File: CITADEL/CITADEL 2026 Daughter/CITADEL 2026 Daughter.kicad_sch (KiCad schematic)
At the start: 4 parts, among them J1 Servo_Daughter

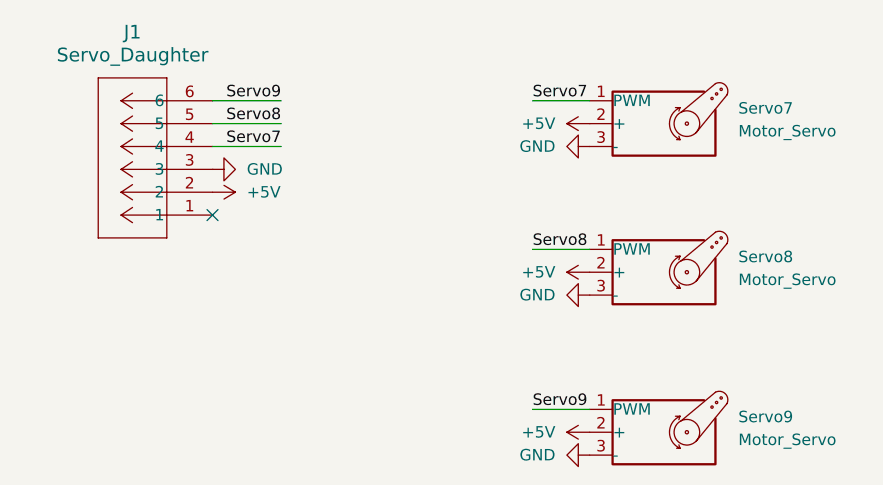
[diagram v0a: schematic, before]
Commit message: Updated servo connectors
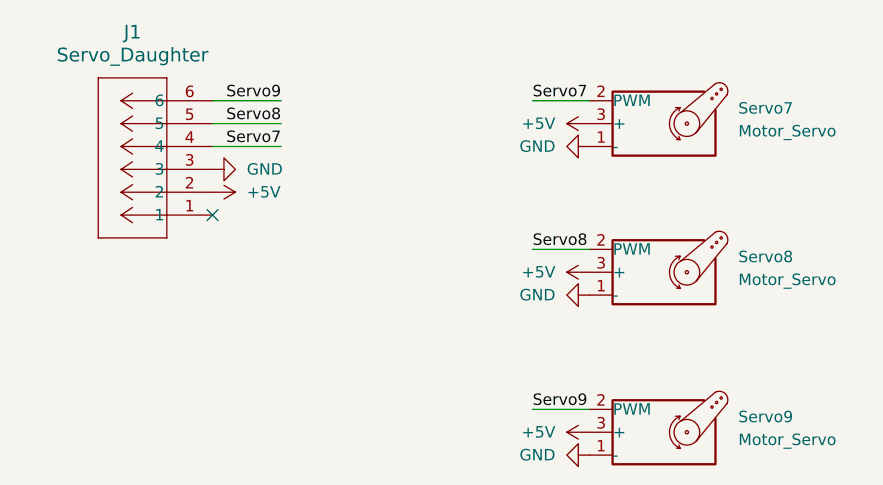
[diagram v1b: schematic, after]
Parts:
- Servo7, Servo8, Servo9: footprint Connector_PinHeader_2.54mm:PinHeader_1x03_P2.54mm_Vertical -> Connector_Molex:Molex_Mini-Fit_Jr_5566-04A_2x02_P4.20mm_Vertical
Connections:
- net +5V: now also Servo7.3 (+), Servo8.3 (+), Servo9.3 (+); no longer Servo7.2 (+), Servo8.2 (+), Servo9.2 (+)
- net GND: now also Servo7.1 (-), Servo8.1 (-), Servo9.1 (-); no longer Servo7.3 (-), Servo8.3 (-), Servo9.3 (-)
- net Servo7: now also Servo7.2 (PWM); no longer Servo7.1 (PWM)
- net Servo8: now also Servo8.2 (PWM); no longer Servo8.1 (PWM)
- net Servo9: now also Servo9.2 (PWM); no longer Servo9.1 (PWM)
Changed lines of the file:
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@@
 	)
 	(symbol
+		(lib_name "Motor_Servo_2")
 		(lib_id "Motor:Motor_Servo")
 		(at 90.17 49.53 0)
@@
 			)
 		)
-		(property "Footprint" "Connector_PinHeader_2.54mm:PinHeader_1x03_P2.54mm_Vertical"
+		(property "Footprint" "Connector_Molex:Molex_Mini-Fit_Jr_5566-04A_2x02_P4.20mm_Vertical"
 			(at 90.17 54.356 0)
 			(effects
@@
 	)
 	(symbol
+		(lib_name "Motor_Servo_1")
 		(lib_id "Motor:Motor_Servo")
 		(at 90.17 33.02 0)
@@
 			)
 		)
-		(property "Footprint" "Connector_PinHeader_2.54mm:PinHeader_1x03_P2.54mm_Vertical"
+		(property "Footprint" "Connector_Molex:Molex_Mini-Fit_Jr_5566-04A_2x02_P4.20mm_Vertical"
 			(at 90.17 37.846 0)
 			(effects
@@
 			)
 		)
-		(property "Footprint" "Connector_PinHeader_2.54mm:PinHeader_1x03_P2.54mm_Vertical"
+		(property "Footprint" "Connector_Molex:Molex_Mini-Fit_Jr_5566-04A_2x02_P4.20mm_Vertical"
 			(at 90.17 72.136 0)
 			(effects

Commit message: Changed layout to support new linear actuators
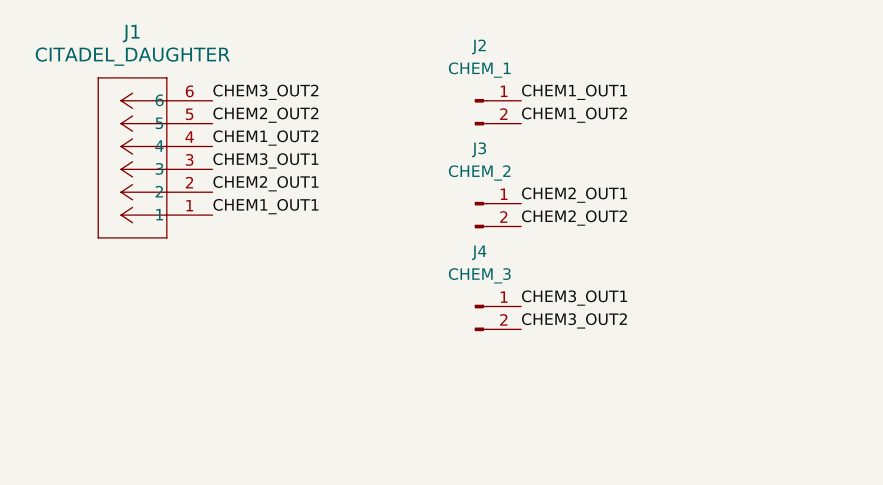
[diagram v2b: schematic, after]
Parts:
- removed Servo7, Servo8, Servo9: Motor_Servo, Connector_Molex:Molex_Mini-Fit_Jr_5566-04A_2x02_P4.20mm_Vertical, symbol Motor:Motor_Servo
- added J2: CHEM_1, Connector_Molex:Molex_Mini-Fit_Jr_5566-02A_2x01_P4.20mm_Vertical, symbol Connector:Conn_01x02_Pin
- added J3: CHEM_2, Connector_Molex:Molex_Mini-Fit_Jr_5566-02A_2x01_P4.20mm_Vertical, symbol Connector:Conn_01x02_Pin
- added J4: CHEM_3, Connector_Molex:Molex_Mini-Fit_Jr_5566-02A_2x01_P4.20mm_Vertical, symbol Connector:Conn_01x02_Pin
- J1: value Servo_Daughter -> CITADEL_DAUGHTER; footprint Jayse_Footprints:CONN_SD-5566-002_06_MOL -> Jayse_Footprints:MOLEX_0039281063
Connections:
- net CHEM1_OUT1: now reaches J1.1
- net CHEM1_OUT1: now also J2.1 (Pin_1)
- net +5V renamed CHEM2_OUT1
- net CHEM2_OUT1: now also J3.1 (Pin_1)
- net GND renamed CHEM3_OUT1
- net CHEM3_OUT1: now also J4.1 (Pin_1)
- net Servo7 renamed CHEM1_OUT2
- net CHEM1_OUT2: now also J2.2 (Pin_2)
- net Servo8 renamed CHEM2_OUT2
- net CHEM2_OUT2: now also J3.2 (Pin_2)
- net Servo9 renamed CHEM3_OUT2
- net CHEM3_OUT2: now also J4.2 (Pin_2)
- no-connect marks 1 -> 0

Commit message: Updated reference names
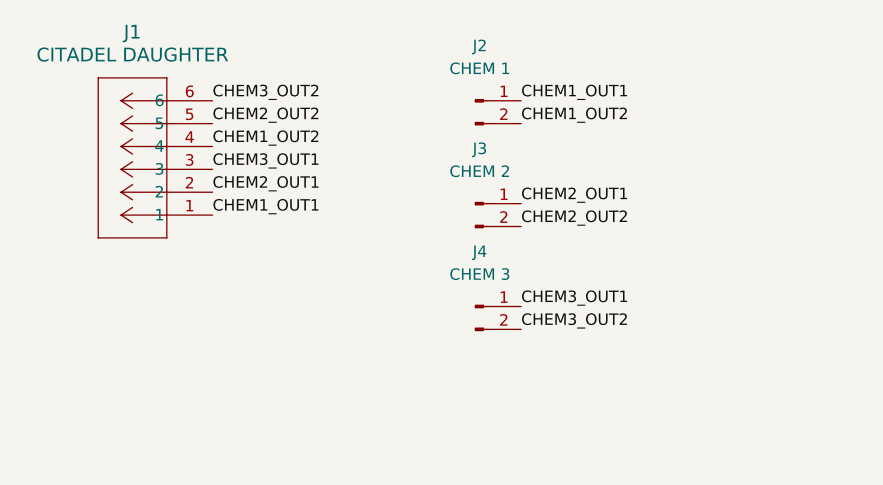
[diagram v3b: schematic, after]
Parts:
- J1: value CITADEL_DAUGHTER -> CITADEL DAUGHTER
- J2: value CHEM_1 -> CHEM 1
- J3: value CHEM_2 -> CHEM 2
- J4: value CHEM_3 -> CHEM 3
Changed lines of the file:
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@@
 			)
 		)
-		(property "Value" "CHEM_1"
+		(property "Value" "CHEM 1"
 			(at 70.358 26.924 0)
 			(effects
@@
 		)
 		(instances
-			(project ""
+			(project "CITADEL 2026 Daughter"
 				(path "/52ce58ca-3d9b-40f7-bd4b-a40ea9b49ff5"
 					(reference "J2")
@@
 			)
 		)
-		(property "Value" "CHEM_3"
+		(property "Value" "CHEM 3"
 			(at 70.358 49.784 0)
 			(effects
@@
 		)
 		(instances
-			(project ""
+			(project "CITADEL 2026 Daughter"
 				(path "/52ce58ca-3d9b-40f7-bd4b-a40ea9b49ff5"
 					(reference "J4")
@@
 			)
 		)
-		(property "Value" "CITADEL_DAUGHTER"
+		(property "Value" "CITADEL DAUGHTER"
 			(at 31.75 25.4 0)
 			(effects
@@
 			)
 		)
-		(property "Value" "CHEM_2"
+		(property "Value" "CHEM 2"
 			(at 70.358 38.354 0)
 			(effects
@@
 		)
 		(instances
-			(project ""
+			(project "CITADEL 2026 Daughter"
 				(path "/52ce58ca-3d9b-40f7-bd4b-a40ea9b49ff5"
 					(reference "J3")
